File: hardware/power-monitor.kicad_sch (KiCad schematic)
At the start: 27 parts, among them J2 Conn_01x04, J3 Screw_Terminal_01x02, J4 Screw_Terminal_01x02, SW1 RESET, U1 INA228, U2 ESP32-C3-WROOM-02, U3 SY8303

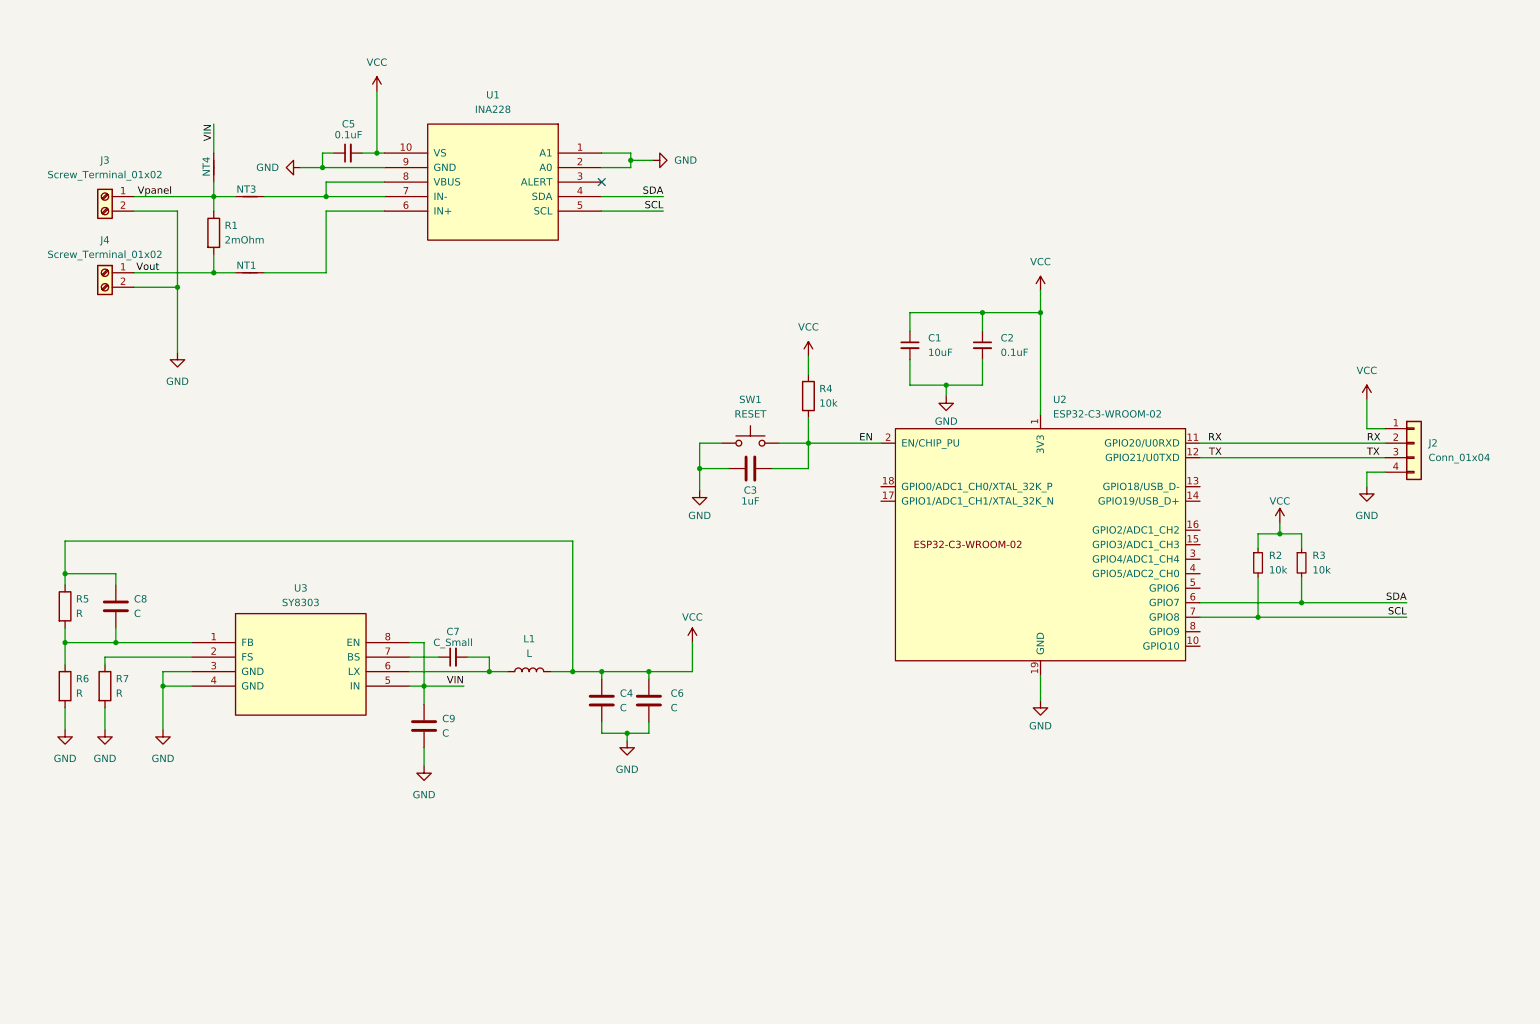
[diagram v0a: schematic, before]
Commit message: PLC based hardware design
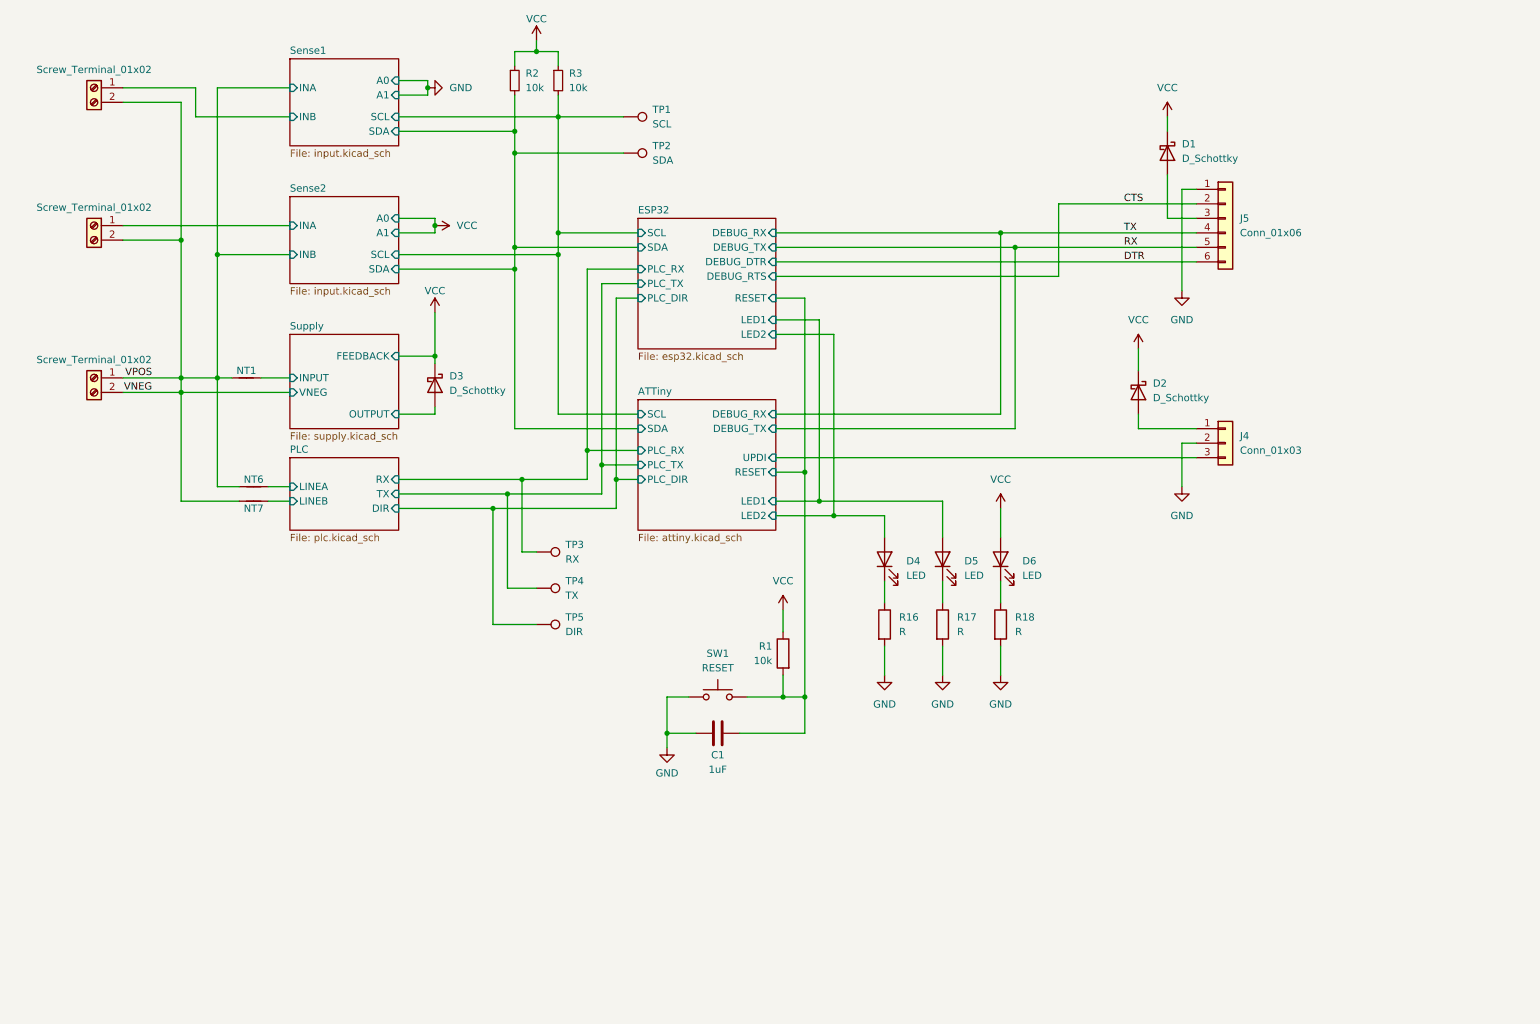
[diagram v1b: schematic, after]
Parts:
- removed C1: 10uF, Capacitor_SMD:C_1206_3216Metric_Pad1.33x1.80mm_HandSolder, symbol Device:C_Small
- removed C2, C5: 0.1uF, Capacitor_SMD:C_1206_3216Metric_Pad1.33x1.80mm_HandSolder, symbol Device:C_Small
- removed C3: 1uF, Capacitor_SMD:C_1206_3216Metric_Pad1.33x1.80mm_HandSolder, symbol Device:C
- removed C4, C6, C8, C9: C, Capacitor_SMD:C_1206_3216Metric_Pad1.33x1.80mm_HandSolder, symbol Device:C
- removed C7: C_Small, Capacitor_SMD:C_1206_3216Metric_Pad1.33x1.80mm_HandSolder, symbol Device:C_Small
- removed J2: Conn_01x04, Connector_PinHeader_2.54mm:PinHeader_1x04_P2.54mm_Horizontal, symbol Connector_Generic:Conn_01x04
- removed J4: Screw_Terminal_01x02, TerminalBlock:TerminalBlock_Altech_AK300-2_P5.00mm, symbol Connector:Screw_Terminal_01x02
- removed L1: L, Inductor_SMD:L_2512_6332Metric_Pad1.52x3.35mm_HandSolder, symbol Device:L
- removed NT3, NT4: NetTie_2, NetTie:NetTie-2_SMD_Pad0.5mm, symbol Device:NetTie_2
- removed R4: 10k, Resistor_SMD:R_1206_3216Metric_Pad1.30x1.75mm_HandSolder, symbol Device:R
- removed R5, R6, R7: R, Resistor_SMD:R_1206_3216Metric_Pad1.30x1.75mm_HandSolder, symbol Device:R
- removed U1: INA228, Package_SO:VSSOP-10_3x3mm_P0.5mm, symbol INA228:INA228
- removed U2: ESP32-C3-WROOM-02, PCM_Espressif:ESP32-C3-WROOM-02, symbol PCM_Espressif:ESP32-C3-WROOM-02
- removed U3: SY8303, Package_TO_SOT_SMD:SOT-23-8, symbol SY8303:SY8303
- added C1: 1uF, Capacitor_SMD:C_1206_3216Metric_Pad1.33x1.80mm_HandSolder, symbol Device:C
- added D1, D2, D3: D_Schottky, Diode_SMD:D_1206_3216Metric_Pad1.42x1.75mm_HandSolder, symbol Device:D_Schottky
- added D4, D5, D6: LED, LED_SMD:LED_1206_3216Metric_Pad1.42x1.75mm_HandSolder, symbol Device:LED
- added J1, J2: Screw_Terminal_01x02, TerminalBlock_Phoenix:TerminalBlock_Phoenix_PT-1,5-2-5.0-H_1x02_P5.00mm_Horizontal, symbol Connector:Screw_Terminal_01x02
- added J4: Conn_01x03, Connector_PinHeader_2.54mm:PinHeader_1x03_P2.54mm_Horizontal, symbol Connector_Generic:Conn_01x03
- added J5: Conn_01x06, Connector_PinHeader_2.54mm:PinHeader_1x06_P2.54mm_Horizontal, symbol Connector_Generic:Conn_01x06
- added NT6, NT7: NetTie_2, NetTie:NetTie-2_SMD_Pad0.5mm, symbol Device:NetTie_2
- added R16, R17, R18: R, Resistor_SMD:R_1206_3216Metric_Pad1.30x1.75mm_HandSolder, symbol Device:R
- added TP1: SCL, TestPoint:TestPoint_Loop_D2.50mm_Drill1.0mm, symbol Connector:TestPoint
- added TP2: SDA, TestPoint:TestPoint_Loop_D2.50mm_Drill1.0mm, symbol Connector:TestPoint
- added TP3: RX, TestPoint:TestPoint_Loop_D2.50mm_Drill1.0mm, symbol Connector:TestPoint
- added TP4: TX, TestPoint:TestPoint_Loop_D2.50mm_Drill1.0mm, symbol Connector:TestPoint
- added TP5: DIR, TestPoint:TestPoint_Loop_D2.50mm_Drill1.0mm, symbol Connector:TestPoint
- J3: footprint TerminalBlock:TerminalBlock_Altech_AK300-2_P5.00mm -> TerminalBlock_Phoenix:TerminalBlock_Phoenix_PT-1,5-2-5.0-H_1x02_P5.00mm_Horizontal
- R1: value 2mOhm -> 10k; footprint Resistor_SMD:R_2512_6332Metric_Pad1.40x3.35mm_HandSolder -> Resistor_SMD:R_1206_3216Metric_Pad1.30x1.75mm_HandSolder
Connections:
- net EN is gone; now on net GND: SW1.2
- net GND: now also C1.2, J4.2 (Pin_2), J5.1 (Pin_1), R16.2, R17.2, R18.2; no longer J3.2 (Pin_2), SW1.1
- net RX: now also J5.5 (Pin_5)
- net TX: now also J5.4 (Pin_4)
- net VCC: now also R1.1, D1.1 (K), D2.1 (K), D3.1 (K), D6.2 (A)
- net Supply/INPUT: now reaches NT1.2
- net SCL renamed ATTiny/SDA
- net ATTiny/SDA: now also TP2.1
- net SDA renamed ATTiny/SCL
- net ATTiny/SCL: now also TP1.1
- net Vout renamed ATTiny/RESET
- net ATTiny/RESET: now also SW1.1, C1.1; no longer NT1.1
- net Vpanel renamed VNEG
- net VNEG: now also J3.2 (Pin_2), NT1.1, J1.2 (Pin_2), J2.2 (Pin_2), NT6.1, NT7.1; no longer R1.1
- new net: D5.1 (K), R17.1
- new net: D1.2 (A), J5.3 (Pin_3)
- new net: D6.1 (K), R18.1
- new net: D4.1 (K), R16.1
- new net: D2.2 (A), J4.1 (Pin_1)
- new net ATTiny/LED1: D5.2 (A)
- new net ATTiny/LED2: D4.2 (A)
- new net ATTiny/PLC_DIR: TP5.1
- new net ATTiny/PLC_RX: TP3.1
- new net ATTiny/PLC_TX: TP4.1
- new net ATTiny/UPDI: J4.3 (Pin_3)
- new net CTS: J5.2 (Pin_2)
- new net DTR: J5.6 (Pin_6)
- new net PLC/LINEA: NT6.2
- new net PLC/LINEB: NT7.2
- new net Sense1/INB: J1.1 (Pin_1)
- new net Sense2/INA: J2.1 (Pin_1)
- new net Supply/OUTPUT: D3.2 (A)
- no-connect marks 1 -> 0
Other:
- added sheet ATTiny (attiny.kicad_sch)
- added sheet ESP32 (esp32.kicad_sch)
- added sheet PLC (plc.kicad_sch)
- added sheet Sense1 (input.kicad_sch)
- added sheet Sense2 (input.kicad_sch)
- added sheet Supply (supply.kicad_sch)

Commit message: Remove PLC, use ESP
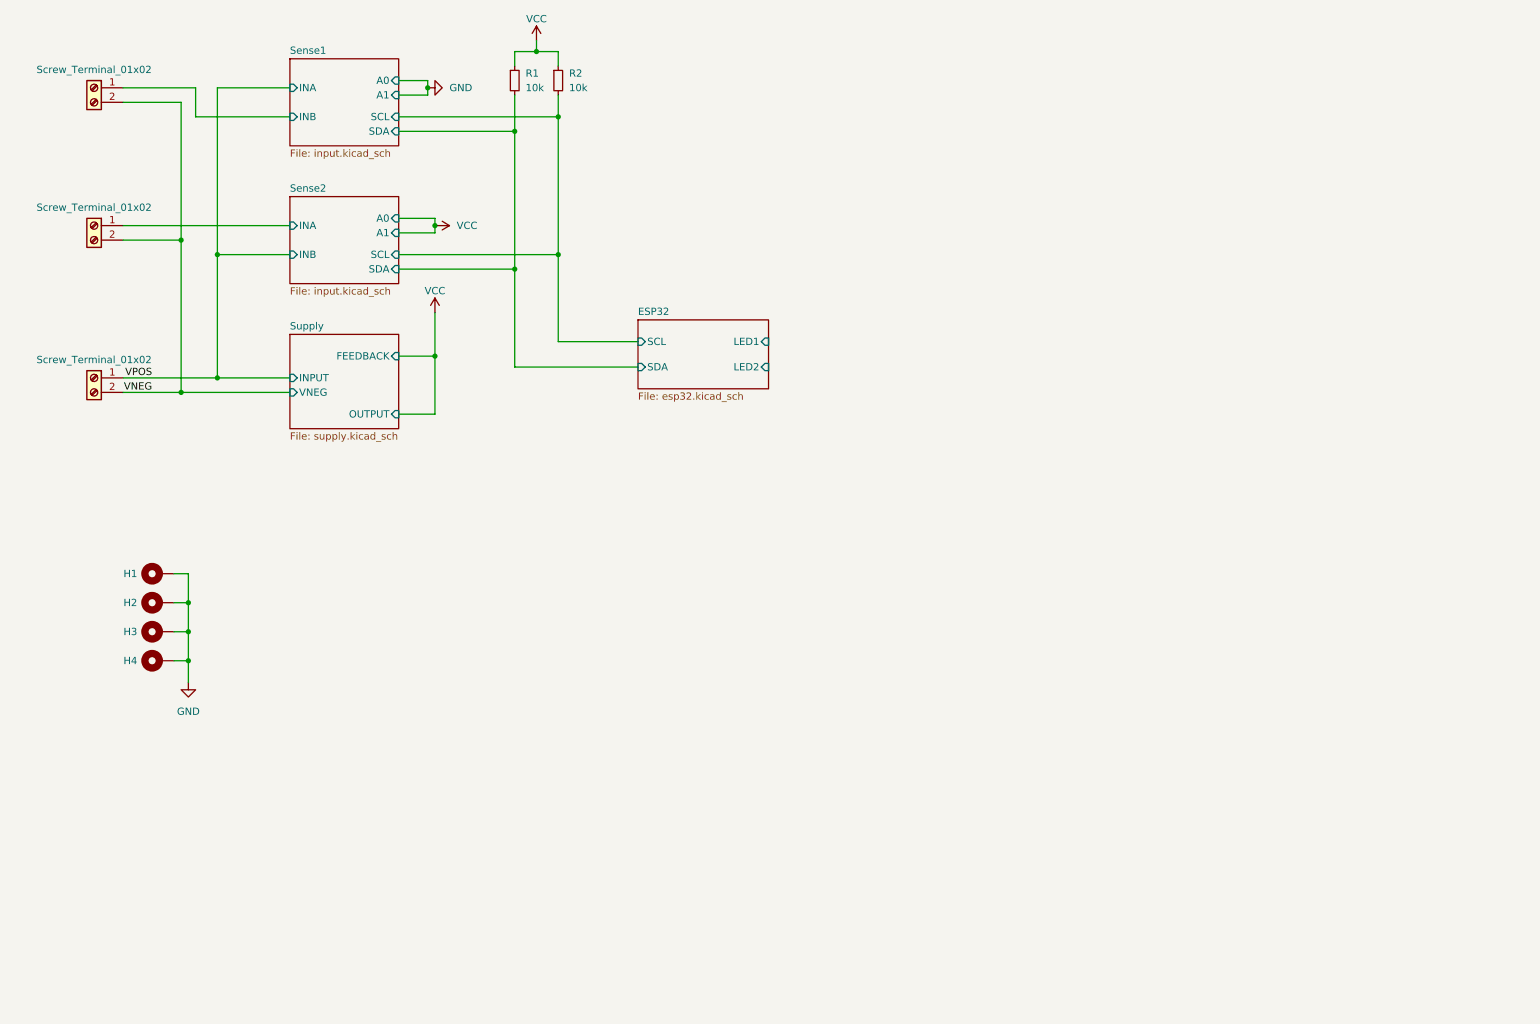
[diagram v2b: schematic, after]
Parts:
- removed C1: 1uF, Capacitor_SMD:C_1206_3216Metric_Pad1.33x1.80mm_HandSolder, symbol Device:C
- removed D1, D2, D3: D_Schottky, Diode_SMD:D_1206_3216Metric_Pad1.42x1.75mm_HandSolder, symbol Device:D_Schottky
- removed D4, D5, D6: LED, LED_SMD:LED_1206_3216Metric_Pad1.42x1.75mm_HandSolder, symbol Device:LED
- removed J4: Conn_01x03, Connector_PinHeader_2.54mm:PinHeader_1x03_P2.54mm_Horizontal, symbol Connector_Generic:Conn_01x03
- removed J5: Conn_01x06, Connector_PinHeader_2.54mm:PinHeader_1x06_P2.54mm_Horizontal, symbol Connector_Generic:Conn_01x06
- removed NT1, NT6, NT7: NetTie_2, NetTie:NetTie-2_SMD_Pad0.5mm, symbol Device:NetTie_2
- removed R1: 10k, Resistor_SMD:R_1206_3216Metric_Pad1.30x1.75mm_HandSolder, symbol Device:R
- removed R16, R17, R18: R, Resistor_SMD:R_1206_3216Metric_Pad1.30x1.75mm_HandSolder, symbol Device:R
- removed SW1: RESET, Button_Switch_SMD:SW_Push_1P1T_NO_6x6mm_H9.5mm, symbol Switch:SW_Push
- removed TP1: SCL, TestPoint:TestPoint_Loop_D2.50mm_Drill1.0mm, symbol Connector:TestPoint
- removed TP2: SDA, TestPoint:TestPoint_Loop_D2.50mm_Drill1.0mm, symbol Connector:TestPoint
- removed TP3: RX, TestPoint:TestPoint_Loop_D2.50mm_Drill1.0mm, symbol Connector:TestPoint
- removed TP4: TX, TestPoint:TestPoint_Loop_D2.50mm_Drill1.0mm, symbol Connector:TestPoint
- removed TP5: DIR, TestPoint:TestPoint_Loop_D2.50mm_Drill1.0mm, symbol Connector:TestPoint
- added H1, H2, H3, H4: MountingHole_Pad, MountingHole:MountingHole_2.2mm_M2_Pad, symbol Mechanical:MountingHole_Pad
- renumbered R2 to R1, R3 to R2
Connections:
- net GND: now also H1.1, H2.1, H3.1, H4.1
- net VNEG: no longer J3.1 (Pin_1)
- net ATTiny/SCL renamed ESP32/SCL
- net ATTiny/SDA renamed ESP32/SDA
- new net VPOS: J3.1 (Pin_1)
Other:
- removed sheet ATTiny
- removed sheet PLC
- sheet ESP32 ports: added none; removed DEBUG_DTR, DEBUG_RTS, DEBUG_RX, DEBUG_TX, PLC_DIR, PLC_RX, PLC_TX, RESET

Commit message: rev 1
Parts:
- removed J1, J2, J3: Screw_Terminal_01x02, TerminalBlock_Phoenix:TerminalBlock_Phoenix_PT-1,5-2-5.0-H_1x02_P5.00mm_Horizontal, symbol Connector:Screw_Terminal_01x02
- removed R1, R2: 10k, Resistor_SMD:R_1206_3216Metric_Pad1.30x1.75mm_HandSolder, symbol Device:R_Small
- added C1: 0.1uF, Capacitor_SMD:C_1206_3216Metric_Pad1.33x1.80mm_HandSolder, symbol Device:C_Small
- added C2: 10uF, Capacitor_SMD:C_1206_3216Metric_Pad1.33x1.80mm_HandSolder, symbol Device:C_Small
- added C3, C9: 0.1uF, Capacitor_SMD:C_0603_1608Metric_Pad1.08x0.95mm_HandSolder, symbol Device:C_Small
- added C4: C, Capacitor_SMD:C_1206_3216Metric_Pad1.33x1.80mm_HandSolder, symbol Device:C
- added D1, D2: LED, LED_SMD:LED_1206_3216Metric_Pad1.42x1.75mm_HandSolder, symbol Device:LED
- added J1: Input A, TerminalBlock_Wuerth:Wuerth_REDCUBE-THR_WP-THRSH_74651175_THR, symbol Connector:Screw_Terminal_01x01
- added J10: I2C, Connector_JST:JST_SH_SM04B-SRSS-TB_1x04-1MP_P1.00mm_Horizontal, symbol Connector_Generic_MountingPin:Conn_01x04_MountingPin
- added J2: Screw_Terminal_01x06, TerminalBlock_Phoenix:TerminalBlock_Phoenix_MPT-0,5-6-2.54_1x06_P2.54mm_Horizontal, symbol Connector:Screw_Terminal_01x06
- added J3: PROG, Connector:Tag-Connect_TC2030-IDC-NL_2x03_P1.27mm_Vertical, symbol symbols:ESP-PROG
- added J4: Output, TerminalBlock_Wuerth:Wuerth_REDCUBE-THR_WP-THRSH_74651175_THR, symbol Connector:Screw_Terminal_01x01
- added J5, J8: Screw_Terminal_01x01, TerminalBlock_Wuerth:Wuerth_REDCUBE-THR_WP-THRSH_74651175_THR, symbol Connector:Screw_Terminal_01x01
- added J6: Ground, TerminalBlock_Wuerth:Wuerth_REDCUBE-THR_WP-THRSH_74651175_THR, symbol Connector:Screw_Terminal_01x01
- added J7: Input B, TerminalBlock_Wuerth:Wuerth_REDCUBE-THR_WP-THRSH_74651175_THR, symbol Connector:Screw_Terminal_01x01
- added J9: I2C, Connector_JST:JST_PH_S4B-PH-SM4-TB_1x04-1MP_P2.00mm_Horizontal, symbol Connector_Generic_MountingPin:Conn_01x04_MountingPin
- added R1, R2: 1k, Resistor_SMD:R_1206_3216Metric_Pad1.30x1.75mm_HandSolder, symbol Device:R
- added R10, R4, R5, R6, R8: 10k, Resistor_SMD:R_1206_3216Metric_Pad1.30x1.75mm_HandSolder, symbol Device:R_Small
- added R12, R3: 2mOhm, Resistor_SMD:R_2816_7142Metric_Pad3.20x4.45mm_HandSolder, symbol Device:R
- added R7: 10k, Resistor_SMD:R_1206_3216Metric_Pad1.30x1.75mm_HandSolder, symbol Device:R
- added SW1: RESET, Button_Switch_SMD:SW_Push_1P1T_NO_6x6mm_H9.5mm, symbol Switch:SW_Push
- added U1: ESP32-C3-WROOM-02-NOTHERMAL, footprints:ESP32-C3-WROOM-02-NOTHERMAL, symbol symbols:ESP32-C3-WROOM-02-NOTHERMAL
- added U2, U4: INA228, Package_SO:VSSOP-10_3x3mm_P0.5mm, symbol symbols:INA228
- renumbered H4 to H1, H1 to H2, H2 to H4
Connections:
- net GND: now also C1.2, C2.2, C3.1, C4.2, C9.1, D1.1 (K), D2.1 (K), J10.1 (Pin_1), J2.1 (Pin_1), J3.4 (GND), J5.1 (Pin_1), J6.1 (Pin_1), J8.1 (Pin_1), J9.1 (Pin_1), SW1.2, U1.9 (GND), U2.1 (A1), U2.2 (A0), U2.7 (GND), U4.7 (GND)
- net VCC: now also C1.1, C2.1, C3.2, C9.2, J10.2 (Pin_2), J2.2 (Pin_2), J3.2 (VDD), J9.2 (Pin_2), R10.1, R4.2, R5.2, R6.2, R7.1, R8.1, U1.1 (3V3), U2.6 (VS), U4.6 (VS)
- net VPOS: now also J4.1 (Pin_1), R12.2, R3.1, U2.10 (Vin+), U4.9 (Vin-)
- new net: J7.1 (Pin_1), R12.1, U4.10 (Vin+), U4.8 (Vbus)
- new net: D2.2 (A), R2.2
- new net: J1.1 (Pin_1), R3.2, U2.8 (Vbus), U2.9 (Vin-)
- new net: D1.2 (A), R1.2
- new net BOOT: J3.6 (BOOT), R4.1, U1.8 (GPIO9)
- new net EN: C4.1, J3.1 (EN), R7.2, SW1.1, U1.2 (EN/CHIP_PU)
- new net EXT0: J2.6 (Pin_6), U1.18 (GPIO0/ADC1_CH0/XTAL_32K_P)
- new net EXT1: J2.5 (Pin_5), U1.17 (GPIO1/ADC1_CH1/XTAL_32K_N)
- new net EXT2: J2.4 (Pin_4), U1.15 (GPIO3/ADC1_CH3)
- new net EXT3: J2.3 (Pin_3), U1.10 (GPIO10)
- new net IO2: R6.1, U1.16 (GPIO2/ADC1_CH2)
- new net IO8: R5.1, U1.7 (GPIO8)
- new net LED1: R1.1, U1.3 (GPIO4/ADC1_CH4)
- new net LED2: R2.1, U1.4 (GPIO5/ADC2_CH0)
- new net RXD: J3.5 (RX), U1.11 (GPIO20/U0RXD)
- new net SCL: J10.4 (Pin_4), J9.4 (Pin_4), R10.2, U1.6 (GPIO7), U2.5 (SCL), U4.5 (SCL)
- new net SDA: J10.3 (Pin_3), J9.3 (Pin_3), R8.2, U1.5 (GPIO6), U2.4 (SDA), U4.1 (A1), U4.2 (A0), U4.4 (SDA)
- new net TXD: J3.3 (TX), U1.12 (GPIO21/U0TXD)
- no-connect marks 0 -> 6
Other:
- removed sheet ESP32
- removed sheet Sense1
- removed sheet Sense2
- sheet Supply ports: added none; removed FEEDBACK, VNEG
- note added: "RXD/TXD are fixed. GPIO2/8/9 are strapping pins and need to be pulled up. All other pins can be swapped."
- moved on the sheet: H1, H2, H3, H4
